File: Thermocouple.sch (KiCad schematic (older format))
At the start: 0 parts

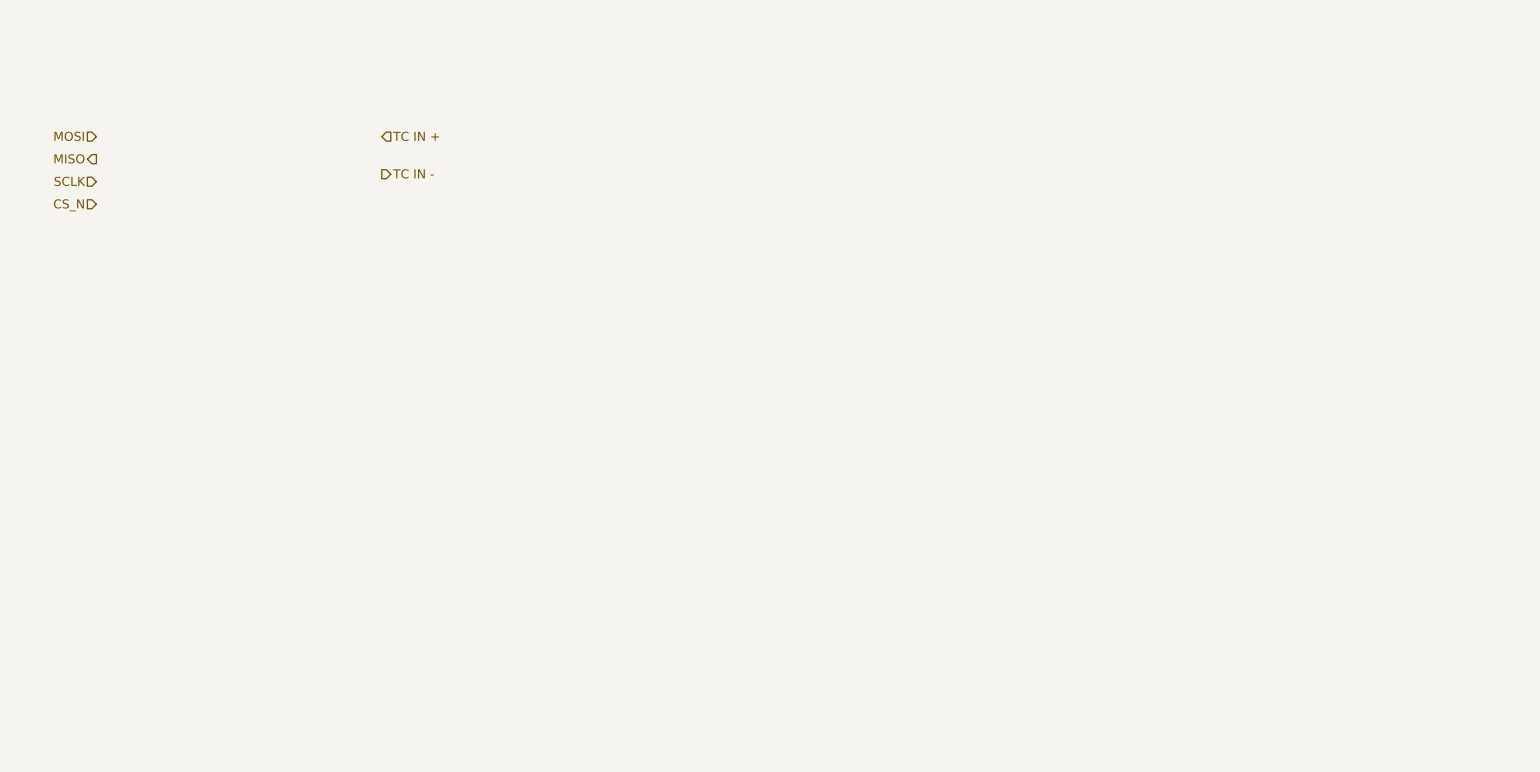
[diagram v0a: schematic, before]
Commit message: M3U3
Added schematic changes from "Understanding The Thermocouple Module"
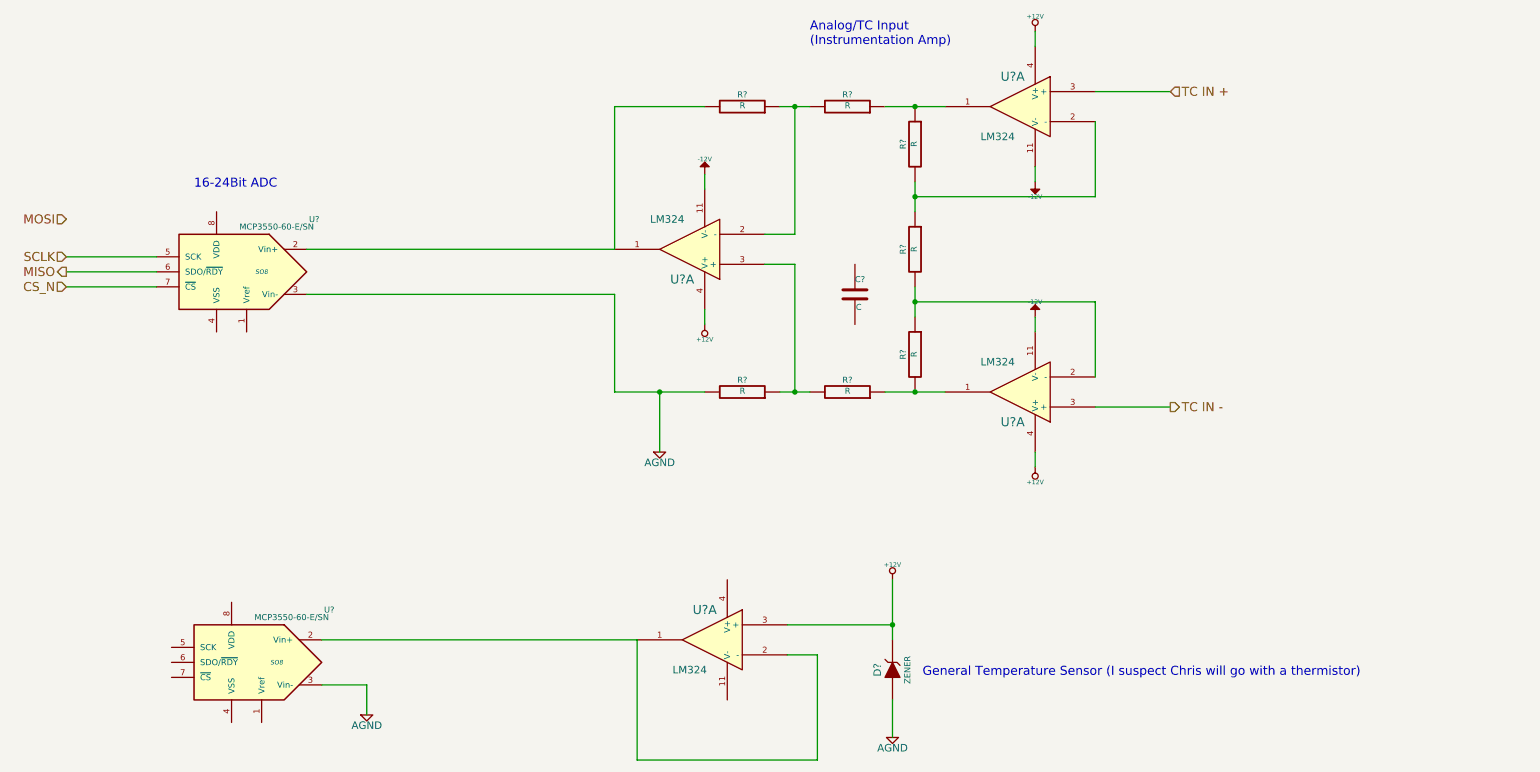
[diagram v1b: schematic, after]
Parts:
- added C?: C, ~, symbol C
- added D?: ZENER, ~, symbol ZENER
- added R? (x7): R, ~, symbol R
- added U? (x4): LM324, symbol LM324
- added U? (x2): MCP3550-60-E/SN, SO8, symbol MCP3550-60-E/SN
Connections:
- net CS_N: now also U?.7 (~CS~)
- net MISO: now also U?.6 (SDO/~RDY~)
- net SCLK: now also U?.5 (SCK)
- net TC IN +: now also U?.3 (+)
- net TC IN -: now also U?.3 (+)
- new net: U?.1, U?.2 (-), U?.2 (Vin+)
- new net: R?.1, R?.2, U?.1
- new net: R?.1, R?.2, U?.2 (-) (x3)
- new net: R?.2, U?.1, U?.2 (Vin+)
- new net: R?.1, R?.2, U?.3 (+)
- new net: R?.1, R?.1, U?.1
- new net +12V: D?.2 (K), U?.3 (+), U?.4 (V+), U?.4 (V+), U?.4 (V+)
- new net -12V: U?.11 (V-), U?.11 (V-), U?.11 (V-)
- new net AGND: D?.1 (A), R?.2, U?.3 (Vin-), U?.3 (Vin-)
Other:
- note added: "16-24Bit ADC"
- note added: "Analog/TC Input \n(Instrumentation Amp)"
- note added: "General Temperature Sensor (I suspect Chris will go with a thermistor)"
